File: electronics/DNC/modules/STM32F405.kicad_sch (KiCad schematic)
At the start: 21 parts

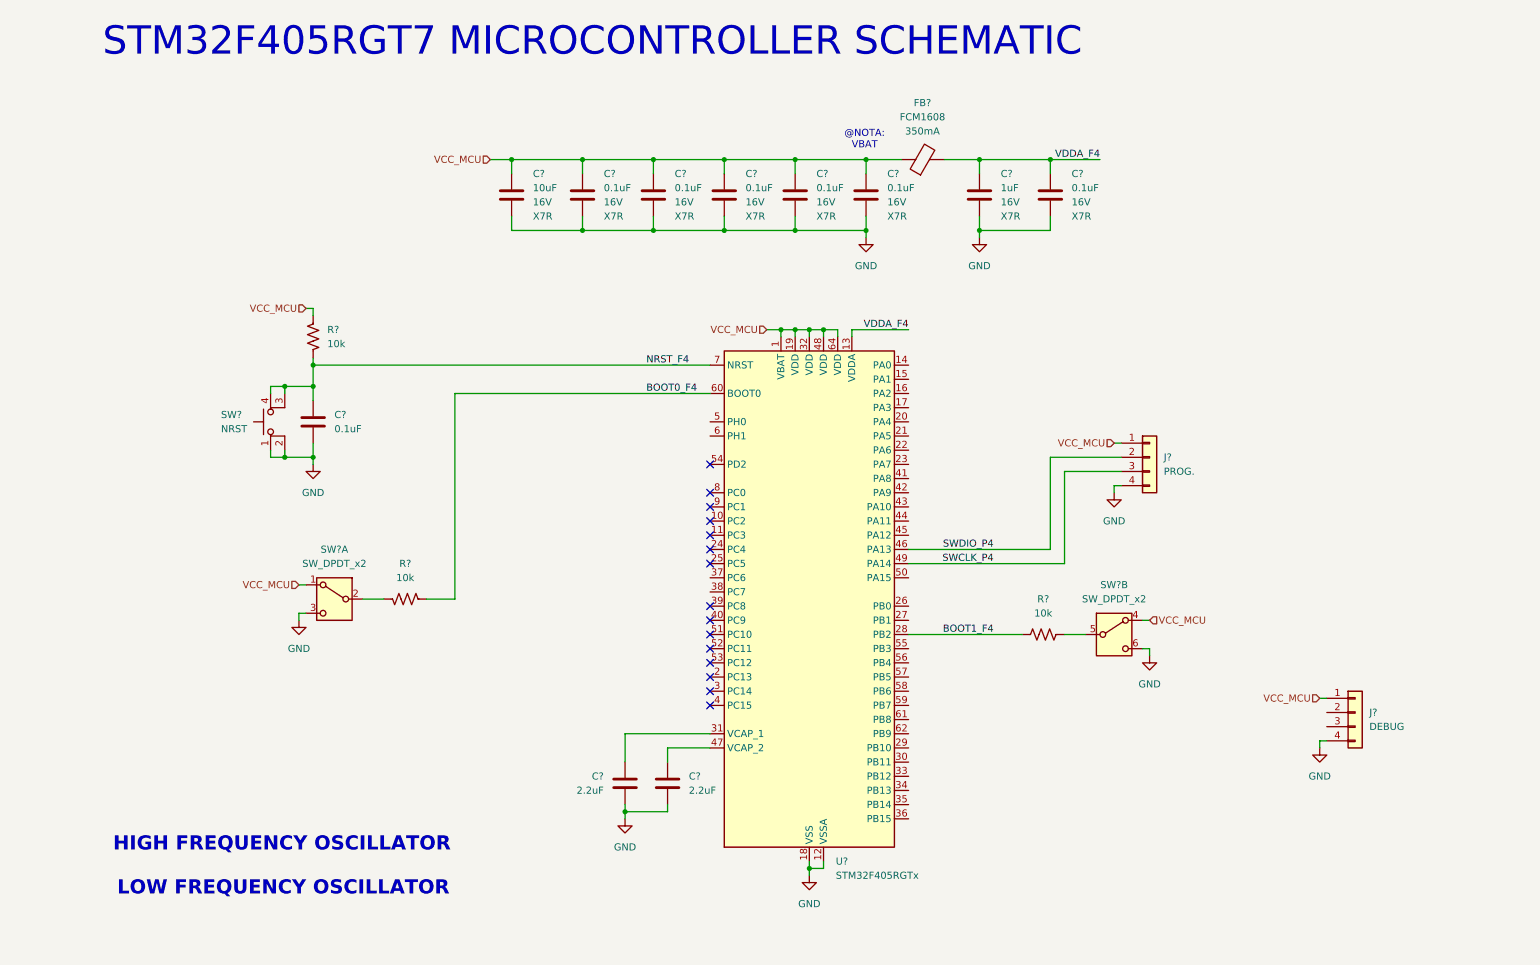
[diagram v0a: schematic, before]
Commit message: Se terminó con el diseño del STM32F4, el PMS, el ESC, el USB-TypeC y el IMU, queda pendiente que la hoja del IMU se cambie por una de sensores.
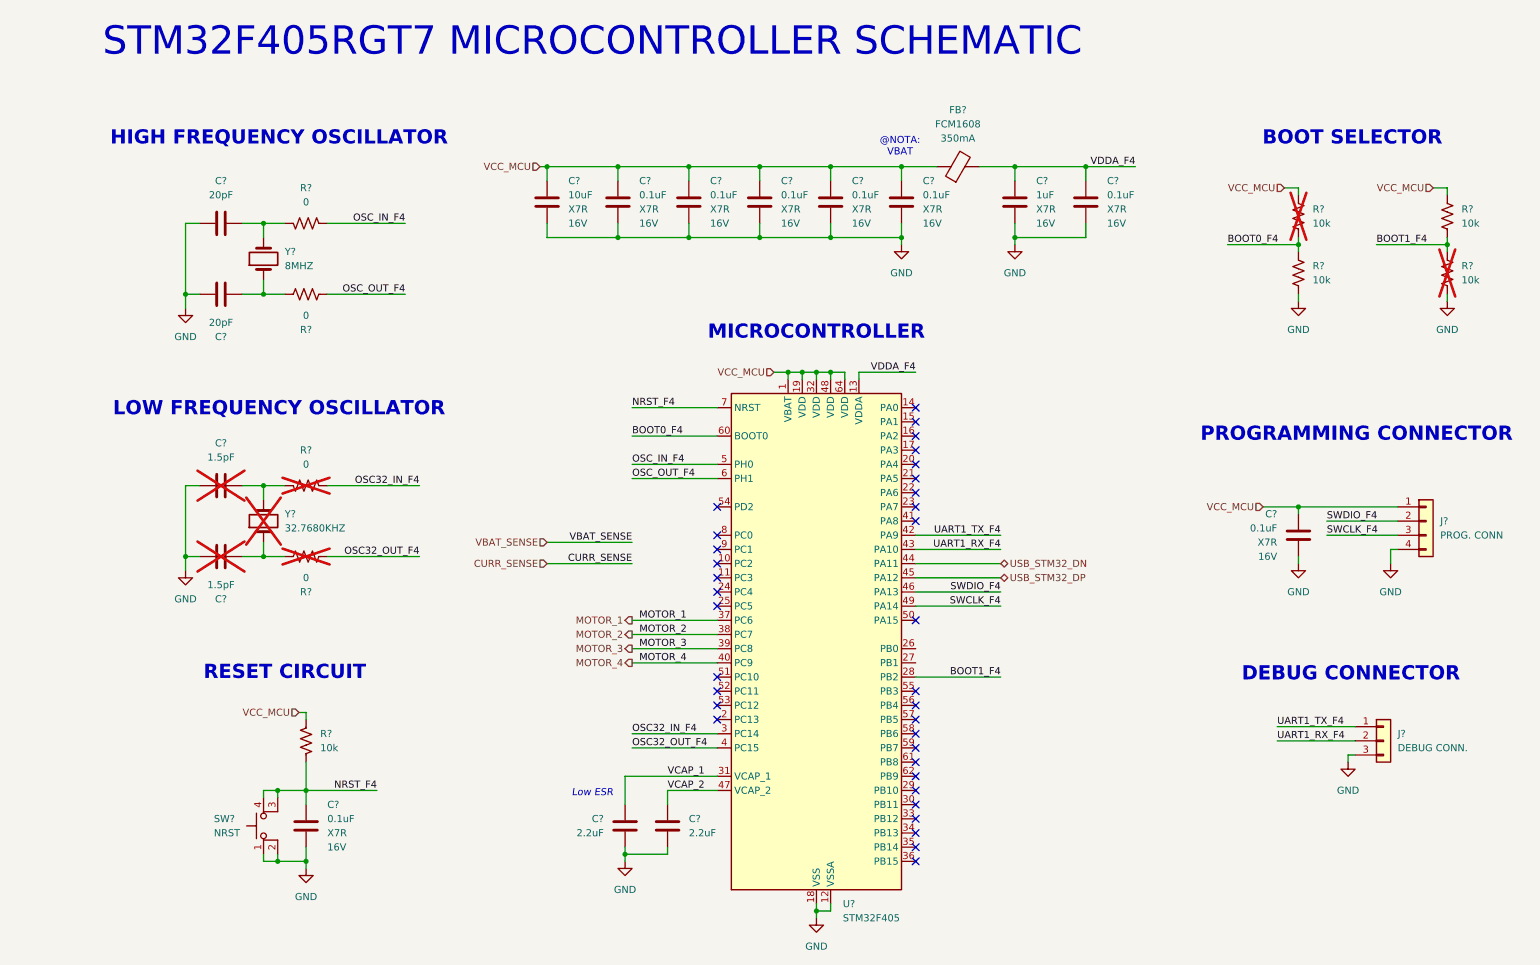
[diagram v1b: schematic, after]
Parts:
- removed C?: 0.1uF, symbol Device:C
- removed SW? (x2): SW_DPDT_x2, symbol Switch:SW_DPDT_x2
- added C? (x2): 1.5pF, symbol Device:C
- added C? (x2): 20pF, symbol Device:C
- added C? (x2): 0.1uF, symbol Device:C
- added R? (x2): 10k, symbol Device:R_US
- added R? (x4): 0, symbol Device:R_US
- added Y?: 32.7680KHZ, symbol Device:Crystal
- added Y?: 8MHZ, symbol Device:Crystal
- C? (x8): VOLTAGE (none) -> 16V; VOLTAJE 16V -> (none)
- FB?: Descrip 600 OHMS @ 100 MHZ 1 POWER, SIGN -> (none)
- J?: value PROG. -> PROG. CONN
- J?: value DEBUG -> DEBUG CONN.; symbol Connector_Generic:Conn_01x04 -> Connector_Generic:Conn_01x03
- R?: now not fitted; now left out of the parts list
- U?: value STM32F405RGTx -> STM32F405; Descrip IC MCU 32BIT 1MB FLASH 64LQFP -> (none)
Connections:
- net BOOT0_F4: now also R?.2
- net BOOT1_F4: now also R?.2
- net GND: now also J?.3 (Pin_3), C?.1, C?.1, C?.2, C?.2, C?.2, C?.2, R?.1, R?.1; no longer J?.4 (Pin_4)
- net NRST_F4: now also C?.1
- net VCC_MCU: now also R?.2, R?.2, C?.1; no longer J?.1 (Pin_1)
- net VCAP_1: now reaches C?.1, U?.31 (VCAP_1)
- net OSC32_IN_F4: now reaches U?.3 (PC14)
- net OSC32_IN_F4: now also R?.2
- net MOTOR_1: now reaches U?.37 (PC6)
- net MOTOR_2: now reaches U?.38 (PC7)
- net MOTOR_3: now reaches U?.39 (PC8)
- net OSC32_OUT_F4: now reaches U?.4 (PC15)
- net OSC32_OUT_F4: now also R?.2
- net MOTOR_4: now reaches U?.40 (PC9)
- net UART1_TX_F4: now reaches U?.42 (PA9)
- net UART1_TX_F4: now also J?.1 (Pin_1)
- net UART1_RX_F4: now reaches U?.43 (PA10)
- net UART1_RX_F4: now also J?.2 (Pin_2)
- net USB_STM32_DN: now reaches U?.44 (PA11)
- net USB_STM32_DP: now reaches U?.45 (PA12)
- net VCAP_2: now reaches C?.1, U?.47 (VCAP_2)
- net OSC_IN_F4: now reaches U?.5 (PH0)
- net OSC_IN_F4: now also R?.2
- net OSC_OUT_F4: now reaches U?.6 (PH1)
- net OSC_OUT_F4: now also R?.2
- net SWCLK_P4 renamed SWCLK_F4
- net SWDIO_P4 renamed SWDIO_F4
- new net: C?.2, R?.1, Y?.2 (x2)
- new net: C?.1, R?.1, Y?.1 (x2)
- no-connect marks 15 -> 34
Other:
- note added: "BOOT SELECTOR"
- note added: "DEBUG CONNECTOR"
- note added: "Low ESR"
- note added: "MICROCONTROLLER"
- note added: "PROGRAMMING CONNECTOR"
- note added: "RESET CIRCUIT"
- company: (none) -> ${COMPANY}
- title: (none) -> ${TITLE}
- moved on the sheet: C?, FB?, J?, R?, SW?, U?
